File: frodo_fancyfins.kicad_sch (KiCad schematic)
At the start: 65 parts, among them J1 Molex MicroFit 2x3, J2 Molex MicroFit 2x3, J3 U.FL, J4 SWD Header, Q1 AO3400A, U1 STM32F072RBTx, U14 AS321KTR-G1, U15 AZ1117-5.0, U16 AZ1117-5.0, U18 W25Q128JVP, U2 MCP2562-E-SN, U3 AZ1117-3.3, Y1 8MHz 12pF

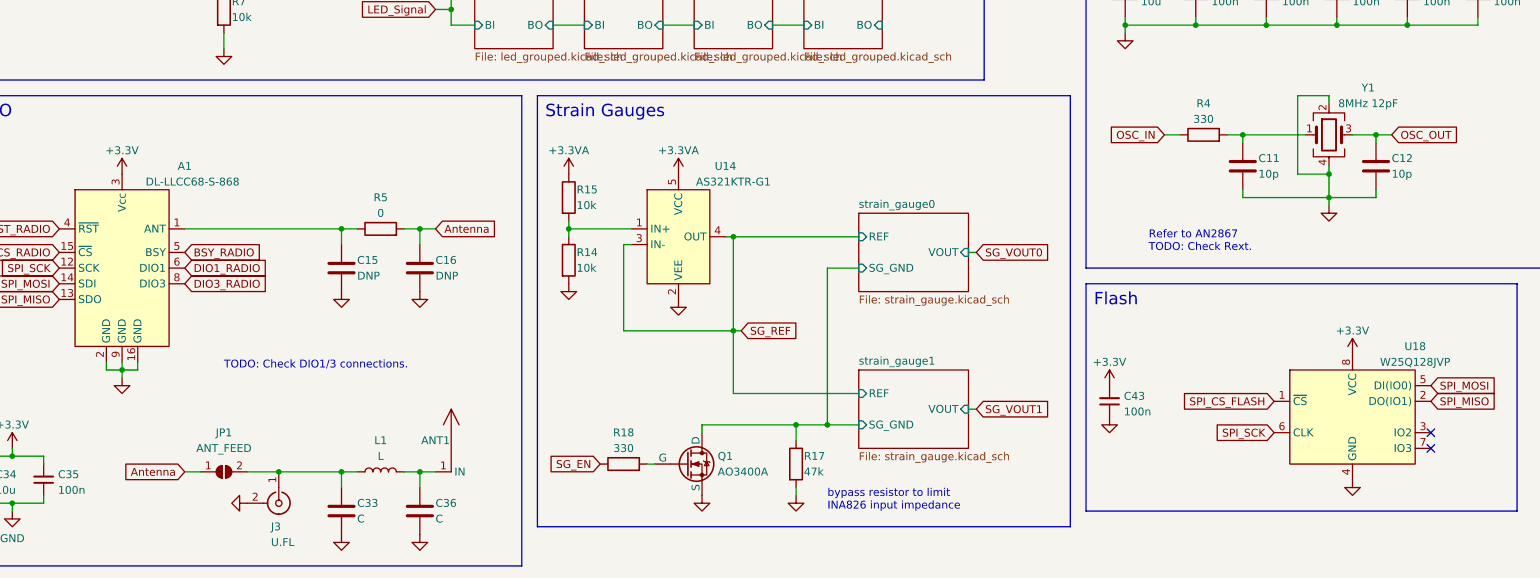
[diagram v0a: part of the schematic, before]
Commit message: Asign footprints, add missing footprints, adjust Rext.
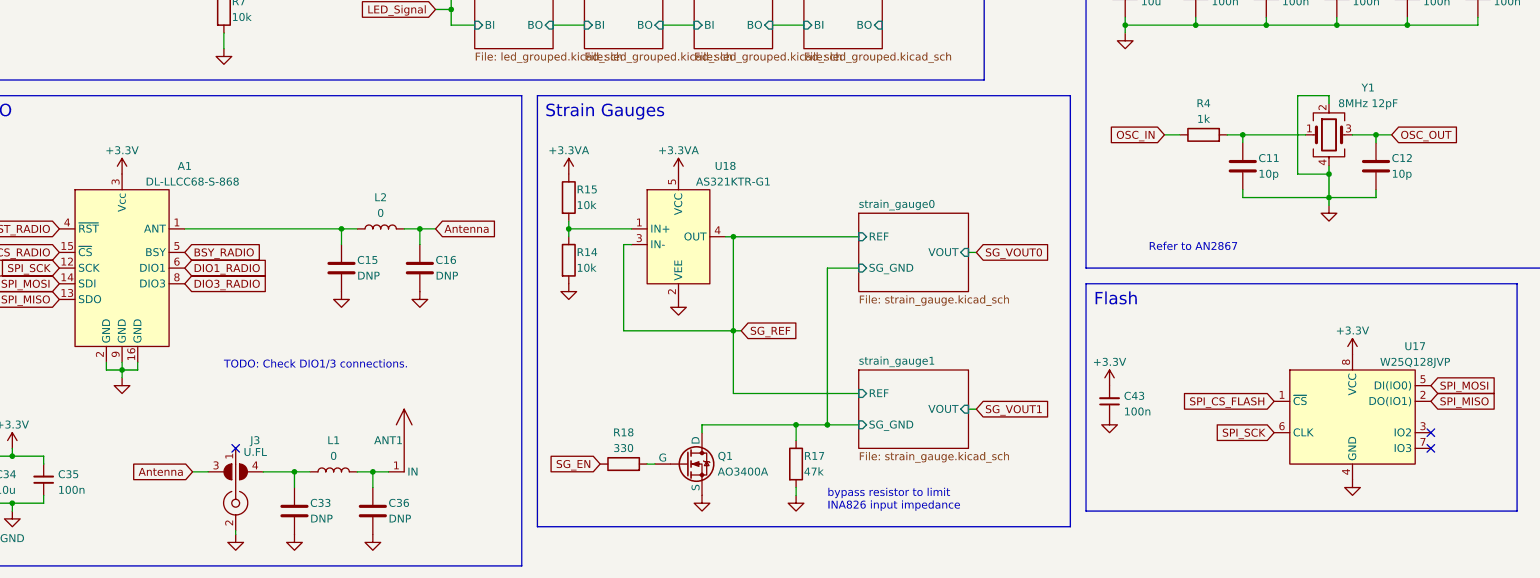
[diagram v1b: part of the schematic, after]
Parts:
- removed J3: U.FL, symbol Connector:Conn_Coaxial
- removed JP1: ANT_FEED, symbol Jumper:SolderJumper_2_Open
- removed R5: 0, symbol Device:R
- removed U14: AS321KTR-G1, symbol frodo_fancyfins:AS321KTR-G1
- removed U18: W25Q128JVP, symbol frodo_fancyfins:W25Q128JVP
- added J3: U.FL, frodo_fancyfins:SolderJumper-U.FL, symbol frodo_fancyfins:SolderJumper-U.FL
- added L2: 0, Inductor_SMD:L_0603_1608Metric_Pad1.05x0.95mm_HandSolder, symbol Device:L
- added U17: W25Q128JVP, Package_SON:WSON-8-1EP_6x5mm_P1.27mm_EP3.4x4.3mm, symbol frodo_fancyfins:W25Q128JVP
- added U18: AS321KTR-G1, frodo_fancyfins:SOT25, symbol frodo_fancyfins:AS321KTR-G1
- C1, C10, C11, C12, C2, C3, C4, C5, C7: footprint (none) -> Capacitor_SMD:C_0402_1005Metric_Pad0.74x0.62mm_HandSolder
- C13, C15, C16, C39, C41, C6, C8, C9: footprint (none) -> Capacitor_SMD:C_0603_1608Metric_Pad1.08x0.95mm_HandSolder
- C14, C40, C42: footprint (none) -> Capacitor_SMD:C_0805_2012Metric_Pad1.18x1.45mm_HandSolder
- C33, C36: value C -> DNP; footprint (none) -> Capacitor_SMD:C_0603_1608Metric_Pad1.08x0.95mm_HandSolder
- C34: footprint Capacitor_SMD:C_1206_3216Metric -> Capacitor_SMD:C_0603_1608Metric_Pad1.08x0.95mm_HandSolder; LCSC# C14860 -> (none); Manufacturer Samsung Electro-Mechanics -> (none); Part# CL31B106KAHNNNE -> (none)
- C35, C43: footprint Capacitor_SMD:C_0603_1608Metric -> Capacitor_SMD:C_0402_1005Metric_Pad0.74x0.62mm_HandSolder; LCSC# C1591 -> (none); Manufacturer Samsung Electro-Mechanics -> (none); Part# CL10B104KB8NNNC -> (none)
- D1, D2: footprint (none) -> LED_SMD:LED_0603_1608Metric_Pad1.05x0.95mm_HandSolder
- D11, D12, D21, D22, D23, D24: footprint (none) -> Diode_SMD:D_SMA
- F1, F2: footprint (none) -> Fuse:Fuse_1812_4532Metric_Pad1.30x3.40mm_HandSolder; Notes (none) -> NOT FINAL FOOTPRINT!
- FB1: footprint (none) -> Inductor_SMD:L_0603_1608Metric_Pad1.05x0.95mm_HandSolder
- J1, J2: footprint (none) -> Connector_Molex:Molex_Micro-Fit_3.0_43045-0600_2x03_P3.00mm_Horizontal
- L1: value L -> 0; footprint (none) -> Inductor_SMD:L_0603_1608Metric_Pad1.05x0.95mm_HandSolder
- Q1: footprint (none) -> Package_TO_SOT_SMD:SOT-23-3
- R1, R14, R15, R17, R18, R3, R7, R8: footprint (none) -> Resistor_SMD:R_0402_1005Metric_Pad0.72x0.64mm_HandSolder
- R16: footprint (none) -> Resistor_SMD:R_0603_1608Metric_Pad0.98x0.95mm_HandSolder
- R2: footprint Resistor_SMD:R_0603_1608Metric -> Resistor_SMD:R_0603_1608Metric_Pad0.98x0.95mm_HandSolder; LCSC# C114640 -> (none); Manufacturer YAGEO -> (none); Part# RC0603FR-07120RL -> (none)
- R4: value 330 -> 1k; footprint (none) -> Resistor_SMD:R_0402_1005Metric_Pad0.72x0.64mm_HandSolder
- U15, U16, U3: footprint (none) -> Package_TO_SOT_SMD:SOT-223-3_TabPin2
- U2: Manufacturer Microchip Technology -> (none); Part# MCP2562-H/SN -> (none)
- Y1: footprint (none) -> Crystal:Crystal_SMD_5032-4Pin_5.0x3.2mm
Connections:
- net +3.3V: now also U17.8 (VCC)
- net +3.3VA: now also U18.5 (VCC)
- net Antenna: now also J3.3, L2.2
- net GND: now also J3.2, U17.4 (GND), U18.2 (VEE)
- net SG_REF: now also U18.3 (IN-), U18.4 (OUT)
- net SPI_CS_FLASH: now also U17.1 (~{CS})
- net SPI_MISO: now also U17.2 (DO(IO1))
- net SPI_MOSI: now also U17.5 (DI(IO0))
- net SPI_SCK: now also U17.6 (CLK)
- net at C33.1, L1.1: now also J3.4
- net at R14.1, R15.2: now also U18.1 (IN+)
- net at A1.1 (ANT), C15.1: now also L2.1
- no-connect marks 2 -> 3
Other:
- note added: "Refer to AN2867"
- note removed: "Refer to AN2867 TODO: Check Rext."
- moved on the sheet: ANT1, C33, C36, L1

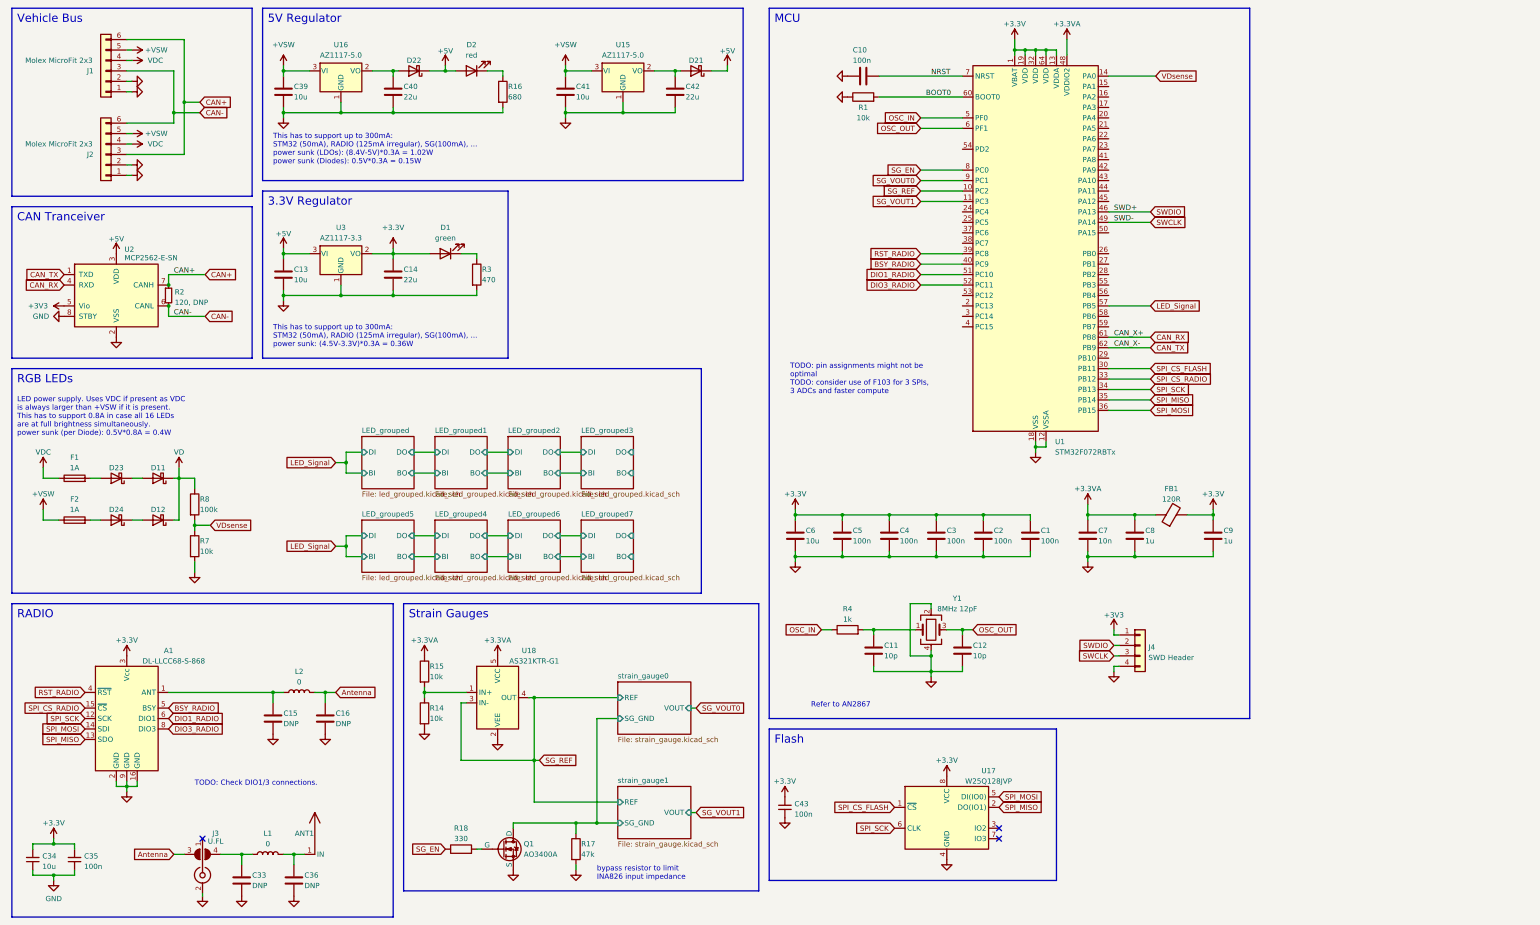
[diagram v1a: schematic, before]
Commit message: Switch from STM32F072 to STM32F103, Add fin shape draft, Place component footprints
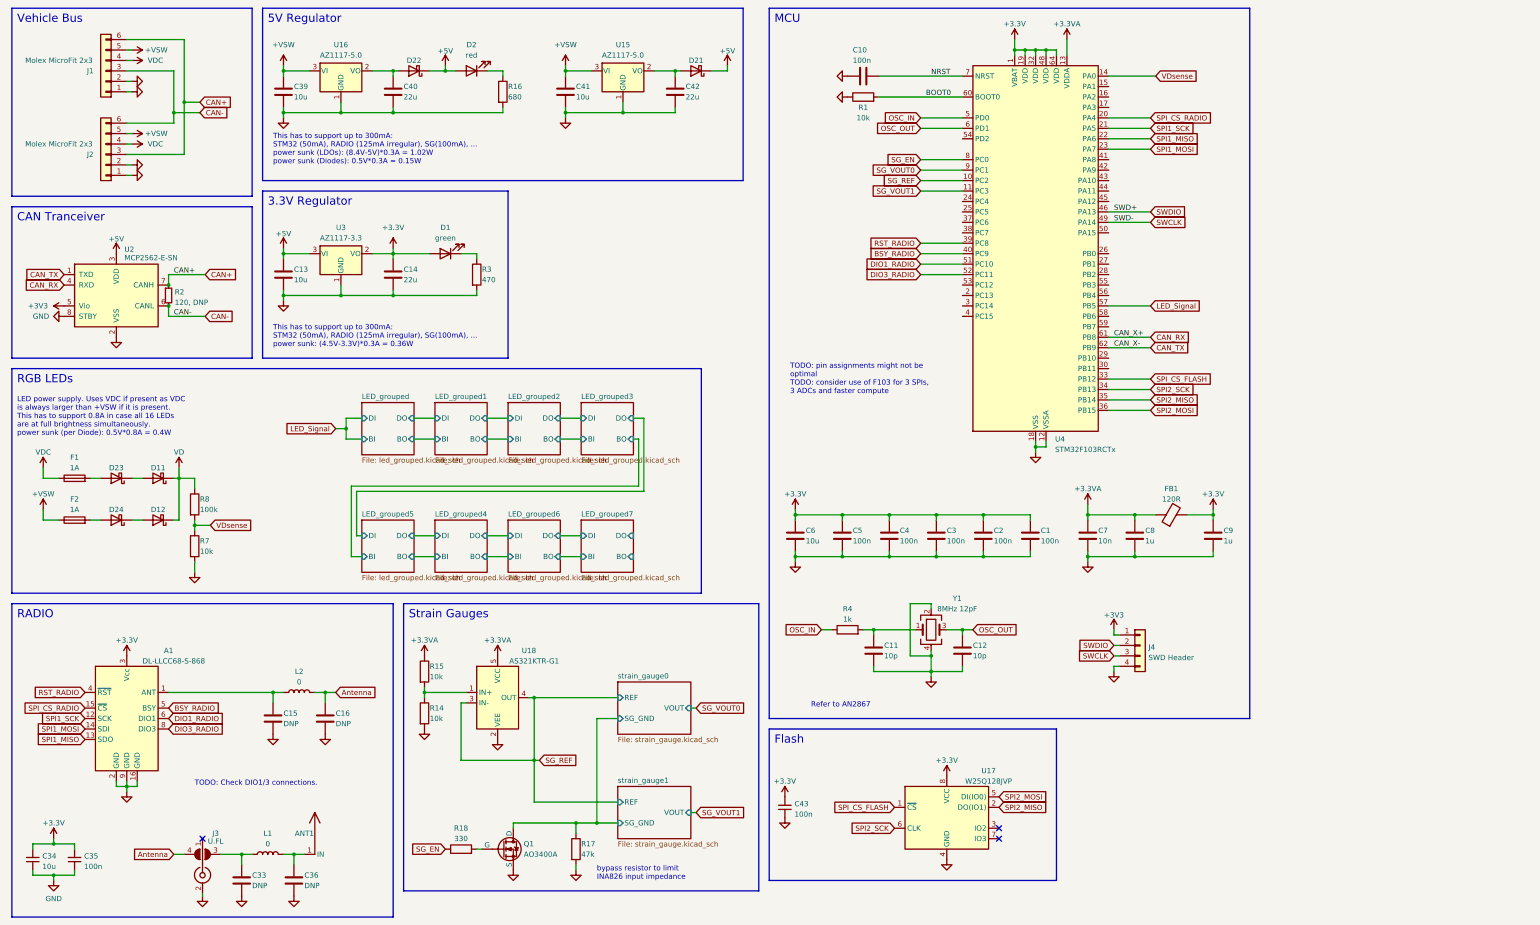
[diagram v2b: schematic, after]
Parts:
- removed U1: STM32F072RBTx, Package_QFP:LQFP-64_10x10mm_P0.5mm, symbol MCU_ST_STM32F0:STM32F072RBTx
- added U4: STM32F103RCTx, Package_QFP:LQFP-64_10x10mm_P0.5mm, symbol MCU_ST_STM32F1:STM32F103RCTx
- J1, J2: footprint Connector_Molex:Molex_Micro-Fit_3.0_43045-0600_2x03_P3.00mm_Horizontal -> Connector_Molex:Molex_Micro-Fit_3.0_43045-0612_2x03_P3.00mm_Vertical
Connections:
- net +3.3V: now also U4.1 (VBAT), U4.19 (VDD), U4.32 (VDD), U4.48 (VDD), U4.64 (VDD)
- net +3.3VA: now also U4.13 (VDDA)
- net Antenna: now also J3.4; no longer J3.3
- net BOOT0: now also U4.60 (BOOT0)
- net BSY_RADIO: now also U4.40 (PC9)
- net CAN_RX: now also U4.61 (PB8)
- net CAN_TX: now also U4.62 (PB9)
- net DIO1_RADIO: now also U4.51 (PC10)
- net DIO3_RADIO: now also U4.52 (PC11)
- net GND: now also U4.12 (VSSA), U4.18 (VSS), U4.31 (VSS), U4.47 (VSS), U4.63 (VSS)
- net LED_Signal: now also U4.57 (PB5)
- net NRST: now also U4.7 (NRST)
- net OSC_IN: now also U4.5 (PD0)
- net OSC_OUT: now also U4.6 (PD1)
- net RST_RADIO: now also U4.39 (PC8)
- net SG_EN: now also U4.8 (PC0)
- net SG_REF: now also U4.10 (PC2)
- net SG_VOUT0: now also U4.9 (PC1)
- net SG_VOUT1: now also U4.11 (PC3)
- net SPI_CS_FLASH: now also U4.33 (PB12)
- net SPI_CS_RADIO: now also U4.20 (PA4)
- net SWCLK: now also U4.49 (PA14)
- net SWDIO: now also U4.46 (PA13)
- net VDsense: now also U4.14 (PA0)
- net at C33.1, L1.1: now also J3.3; no longer J3.4
- net SPI_MISO renamed SPI1_MISO
- net SPI1_MISO: now also U4.22 (PA6); no longer U17.2 (DO(IO1))
- net SPI_MOSI renamed SPI1_MOSI
- net SPI1_MOSI: now also U4.23 (PA7); no longer U17.5 (DI(IO0))
- net SPI_SCK renamed SPI1_SCK
- net SPI1_SCK: now also U4.21 (PA5); no longer U17.6 (CLK)
- new net SPI2_MISO: U17.2 (DO(IO1)), U4.35 (PB14)
- new net SPI2_MOSI: U17.5 (DI(IO0)), U4.36 (PB15)
- new net SPI2_SCK: U17.6 (CLK), U4.34 (PB13)

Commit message: PCB Layout (traces, edge cuts, silk screen, 3d models)
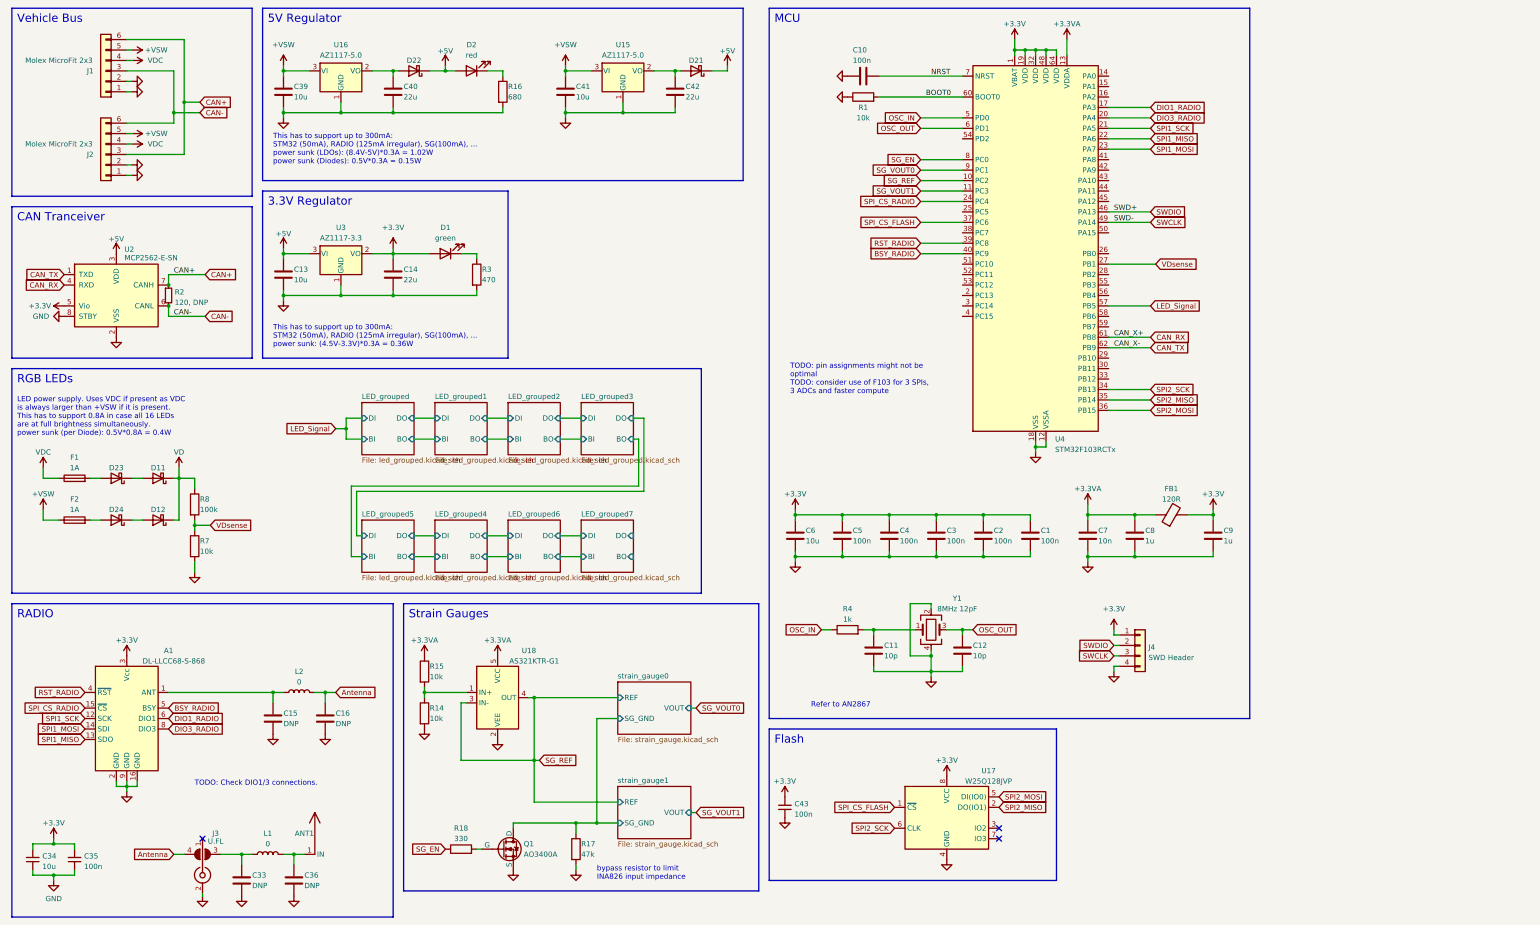
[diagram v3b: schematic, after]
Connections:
- net +3V3 is gone; now on net +3.3V: J4.1 (Pin_1), U2.5 (Vio)
- net DIO1_RADIO: now also U4.17 (PA3); no longer U4.51 (PC10)
- net DIO3_RADIO: now also U4.20 (PA4); no longer U4.52 (PC11)
- net SPI_CS_FLASH: now also U4.37 (PC6); no longer U4.33 (PB12)
- net SPI_CS_RADIO: now also U4.24 (PC4); no longer U4.20 (PA4)
- net VDsense: now also U4.27 (PB1); no longer U4.14 (PA0)
